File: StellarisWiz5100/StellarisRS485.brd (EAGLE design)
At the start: 86 x 84.4 mm, 10 parts

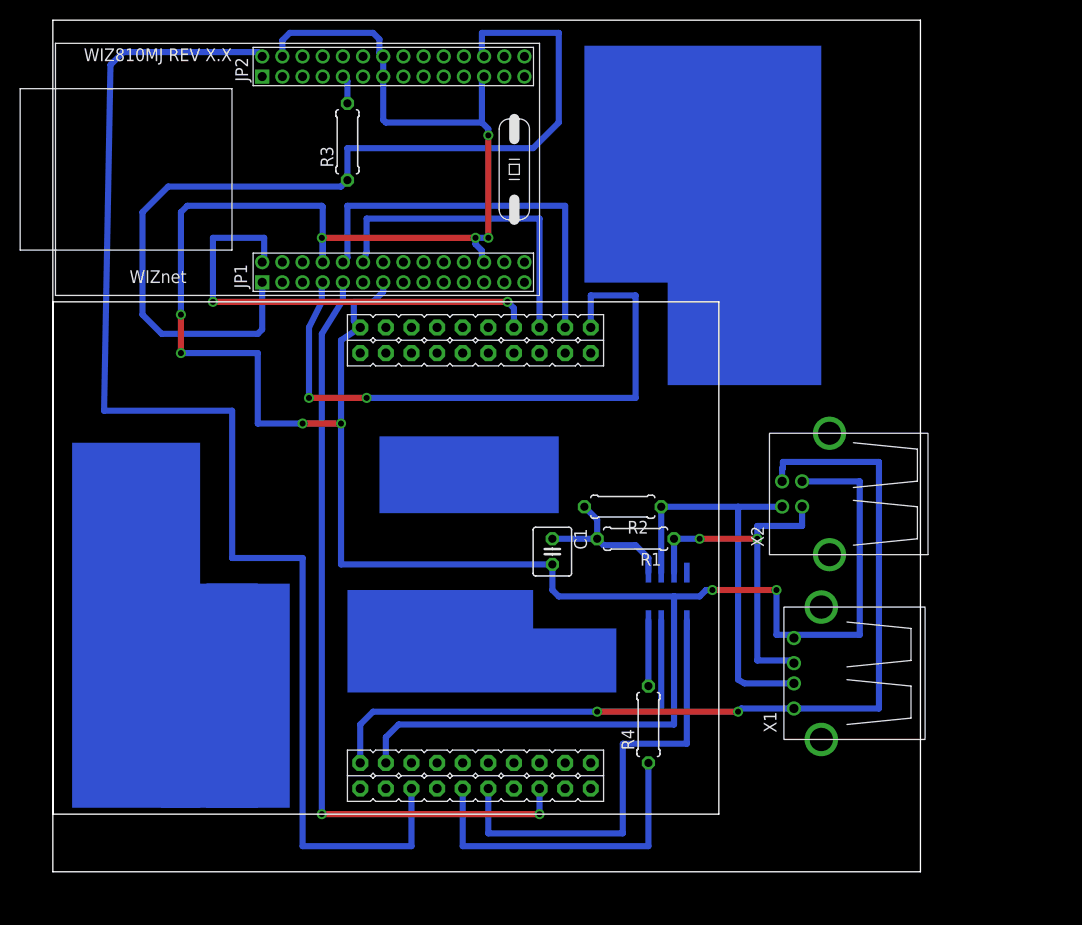
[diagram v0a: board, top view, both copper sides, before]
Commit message: 
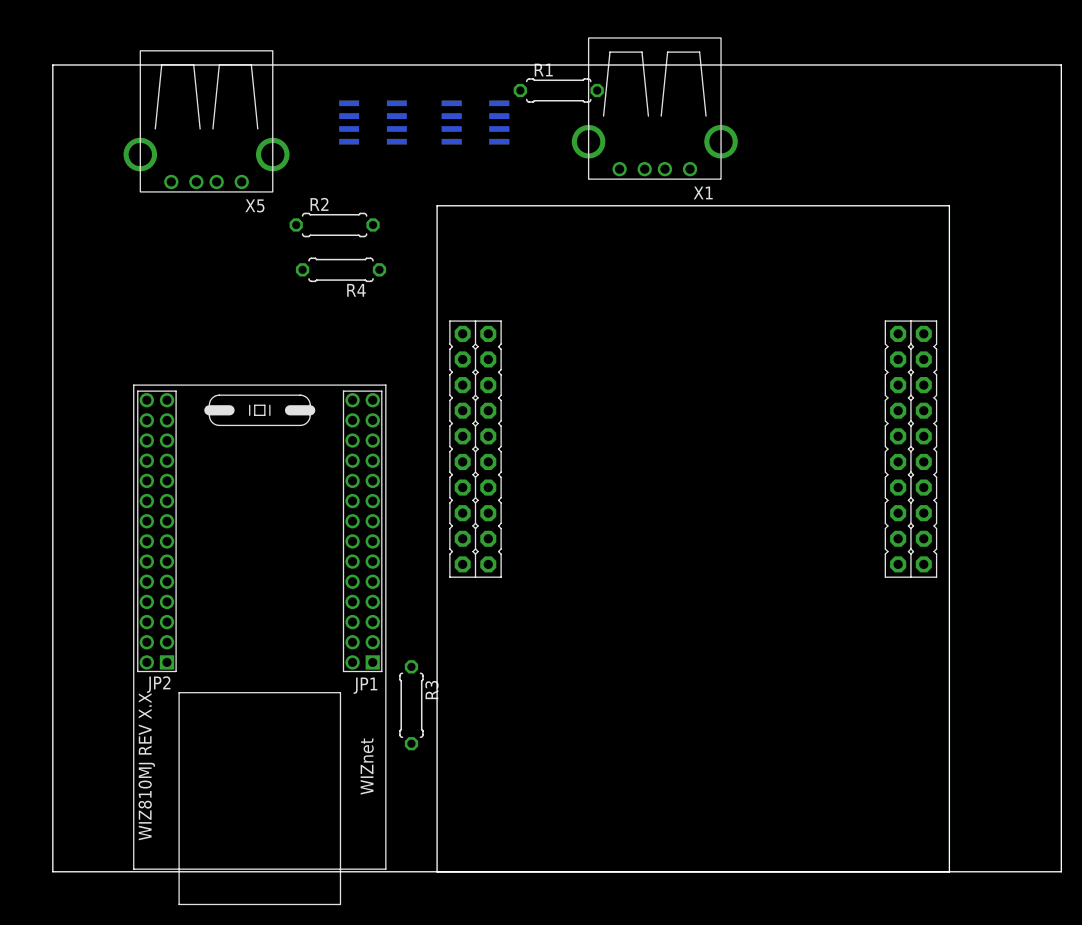
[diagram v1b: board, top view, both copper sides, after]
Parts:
- removed C1: (no value), rcl:C025-040X050
- removed X2: (no value), lieven:USB-B-H
- added U$4: TJA1040, lieven:SOIC8-N_MC
- added X5: (no value), lieven:USB-A-H
- R1, R2, R4: value 60 -> (none)
- moved U$1 89.1 mm to (88.9, 0.00), turned to 90 degrees
- moved R3 56.2 mm to (35.6, 16.5), turned to 270 degrees
- moved X1 55.2 mm to (59.7, 72.4), turned to 270 degrees
- moved R4 54.4 mm to (28.6, 59.7), turned to 180 degrees
- moved U$3 50.7 mm to (41.9, 74.3), turned to 180 degrees
- moved R1 45.1 mm to (50.2, 77.5), turned to 0 degrees
- moved R2 40.0 mm to (27.9, 64.1), turned to 0 degrees
- moved U$2 17.6 mm to (33.0, 48.3), turned to 270 degrees
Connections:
- removed net N$12: R2.1, U$3.6, X1.D-, X2.D-
- removed net N$13: U$1.PB6, U$2.2
- new net N$17: U$1.PB0, U$3.4
- new net N$18: R4.2, U$4.6, X5.D-
- new net N$19: U$1.PB5, U$4.1
- new net N$20: U$1.PB4, U$4.4
- net +5V: now also U$4.3, X5.VBUS; no longer X2.VBUS
- net GND: now also U$4.2, X5.GND; no longer C1.2, X2.GND
- net N$1: now also U$1.PA6; no longer U$1.PB0
- net N$11: now also R4.1, U$4.5; no longer C1.1, R1.2, U$3.5
- net N$2: now also R1.1, U$3.7, X1.D+; no longer R4.2, U$3.4
- net N$4: now also U$3.6, X1.D-; no longer R4.1, U$1.PE4
- net N$5: now also R2.1, U$4.7, X5.D+; no longer R1.1, U$3.7, X1.D+, X2.D+
- net N$7: now also U$1.PB1; no longer U$1.PE5
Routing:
- net GND: track 280.7 -> 0.00 mm, vias 10 -> 0
- net N$1: track 129.4 -> 0.00 mm
- net +5V: track 107.3 -> 0.00 mm, vias 2 -> 0
- net VCC: track 93.4 -> 0.00 mm
- net N$6: track 77.5 -> 0.00 mm, vias 2 -> 0
- net N$3: track 61.9 -> 0.00 mm, vias 2 -> 0
- net N$13: track 45.9 -> 0.00 mm, vias 2 -> 0
- net N$7: track 45.3 -> 0.00 mm
- net N$12: track 41.3 -> 0.00 mm
- net N$9: track 39.4 -> 0.00 mm
- net N$5: track 35.2 -> 0.00 mm, vias 2 -> 0
- net N$4: track 32.4 -> 0.00 mm
- net N$8: track 32.3 -> 0.00 mm
- net N$11: track 15.5 -> 0.00 mm
- net N$2: track 6.53 -> 0.00 mm
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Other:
- board size 86 x 84.4 mm -> 100 x 80 mm
